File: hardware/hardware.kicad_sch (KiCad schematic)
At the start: 8 parts, among them J1 Conn_01x03_Pin, J2 Conn_01x03_Pin, J3 Conn_01x03_Pin, J4 Conn_01x03_Pin, J5 Conn_01x03_Pin, J6 Conn_01x04_Pin, U1 ESP32-DEVKITC-32D

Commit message: feat: hardware schematic
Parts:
- added C1: C_Polarized, symbol Device:C_Polarized
- added IR1, IR2: Conn_01x03_Pin, symbol Connector:Conn_01x03_Pin
- added L7805: L7805, Package_TO_SOT_THT:TO-220-3_Vertical, symbol Regulator_Linear:L7805
- added PW: Screw_Terminal_01x02, TerminalBlock:TerminalBlock_bornier-2_P5.08mm, symbol Connector:Screw_Terminal_01x02
- added TCS: Conn_01x06_Pin, symbol Connector:Conn_01x06_Pin
- added TIP3055: TIP3055G, Package_TO_SOT_THT:TO-247-3_Vertical, symbol Transistor_BJT:TIP3055G
- renumbered J6 to MP01, J1 to SM1, J2 to SM2, J3 to SM3, J4 to SM4, J5 to SM5
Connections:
- net at SM5.1 (Pin_1): now also U1.J2-15 (IO13)
- net at A1.2 (VDD), SM1.2 (Pin_2), SM2.2 (Pin_2)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: now also C1.1, IR1.1 (Pin_1), IR2.1 (Pin_1), TCS.1 (Pin_1), TIP3055.3 (E)
- net at A1.1 (GND), SM1.3 (Pin_3), SM2.3 (Pin_3)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: now also A1.7 (GND), C1.2, IR1.2 (Pin_2), IR2.2 (Pin_2), L7805.2 (GND), PW.2 (Pin_2), TCS.2 (Pin_2)
- net at SM3.1 (Pin_1): now also U1.J2-8 (IO33)
- net at SM1.1 (Pin_1): now also U1.J2-6 (IO35)
- net at A1.13 (~{RESET}): now also A1.14 (~{SLEEP})
- net at A1.15 (STEP): now also U1.J2-12 (IO14)
- net at A1.16 (DIR): now also U1.J2-13 (IO12)
- net at A1.8 (VMOT): now also L7805.1 (IN), PW.1 (Pin_1), TIP3055.2 (C)
- net at SM2.1 (Pin_1): now also U1.J2-7 (IO32)
- net at SM4.1 (Pin_1): now also U1.J2-11 (IO27)
- net at U1.J3-3 (IO22): now also TCS.4 (Pin_4)
- net at U1.J3-6 (IO21): now also TCS.5 (Pin_5)
- net at U1.J3-8 (IO19): now also IR1.3 (Pin_3)
- net at U1.J3-9 (IO18): now also IR2.3 (Pin_3)
- new net: L7805.3 (OUT), TIP3055.1 (B)
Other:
- moved on the sheet: A1, MP01, SM1, SM2, SM3, SM4, SM5, U1

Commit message: feat: added footprints
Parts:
- C1: footprint (none) -> Capacitor_THT:CP_Radial_D5.0mm_P2.50mm
- IR1, IR2, SM1, SM2, SM3, SM4, SM5: footprint (none) -> Connector_PinHeader_2.54mm:PinHeader_1x03_P2.54mm_Vertical
- MP1: renamed from MP01; footprint (none) -> Connector_PinHeader_2.54mm:PinHeader_1x04_P2.54mm_Vertical
- TCS1: renamed from TCS; footprint (none) -> Connector_PinHeader_2.54mm:PinHeader_1x06_P2.54mm_Vertical
- renumbered PW to PW1
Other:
- moved on the sheet: SM2
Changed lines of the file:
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@@
 (kicad_sch (version 20230121) (generator eeschema)
   (paper "A4")
-  (junction (at 59.69 64.77) (diameter 0) (color 0 0 0 0)
+  (junction (at 60.96 66.04) (diameter 0) (color 0 0 0 0)
   )
   (junction (at 152.4 132.08) (diameter 0) (color 0 0 0 0)
@@
   (junction (at 152.4 124.46) (diameter 0) (color 0 0 0 0)
   )
-  (junction (at 60.96 67.31) (diameter 0) (color 0 0 0 0)
-  )
   (junction (at 60.96 99.06) (diameter 0) (color 0 0 0 0)
   )
+  (junction (at 59.69 63.5) (diameter 0) (color 0 0 0 0)
+  )
   (junction (at 60.96 88.9) (diameter 0) (color 0 0 0 0)
   )
@@
     (stroke (width 0) (type default))
   )
-  (wire (pts (xy 60.96 67.31) (xy 60.96 78.74))
+  (wire (pts (xy 60.96 66.04) (xy 60.96 78.74))
     (stroke (width 0) (type default))
   )
@@
     (stroke (width 0) (type default))
   )
-  (wire (pts (xy 59.69 64.77) (xy 59.69 76.2))
+  (wire (pts (xy 59.69 63.5) (xy 59.69 76.2))
     (stroke (width 0) (type default))
   )
@@
     (stroke (width 0) (type default))
   )
-  (wire (pts (xy 60.96 67.31) (xy 60.96 55.88))
-    (stroke (width 0) (type default))
-  )
   (wire (pts (xy 58.42 123.19) (xy 58.42 119.38))
     (stroke (width 0) (type default))
@@
     (stroke (width 0) (type default))
   )
-  (wire (pts (xy 59.69 53.34) (xy 59.69 64.77))
+  (wire (pts (xy 59.69 53.34) (xy 59.69 63.5))
     (stroke (width 0) (type default))
   )
@@
     (stroke (width 0) (type default))
   )
-  (wire (pts (xy 59.69 64.77) (xy 57.15 64.77))
+  (wire (pts (xy 59.69 63.5) (xy 57.15 63.5))
     (stroke (width 0) (type default))
   )
@@
     (stroke (width 0) (type default))
   )
-  (wire (pts (xy 57.15 67.31) (xy 60.96 67.31))
+  (wire (pts (xy 57.15 66.04) (xy 60.96 66.04))
     (stroke (width 0) (type default))
   )
@@
     (stroke (width 0) (type default))
   )
+  (wire (pts (xy 60.96 66.04) (xy 60.96 55.88))
+    (stroke (width 0) (type default))
+  )
   (wire (pts (xy 86.36 58.42) (xy 119.38 58.42))
     (stroke (width 0) (type default))
@@
   )
   (wire (pts (xy 58.42 124.46) (xy 64.77 124.46))
-    (stroke (width 0) (type default))
-  )
-  (wire (pts (xy 57.15 60.96) (xy 57.15 62.23))
     (stroke (width 0) (type default))
   )
@@
   (symbol (lib_id "Connector:Conn_01x04_Pin") (at 52.07 120.65 0) (unit 1)
     (in_bom yes) (on_board yes) (dnp no) (fields_autoplaced)
-    (property "Reference" "MP01" (at 52.705 113.03 0)
+    (property "Reference" "MP1" (at 52.705 113.03 0)
       (effects (font (size 1.27 1.27)))
     )
@@
       (effects (font (size 1.27 1.27)) hide)
     )
-    (property "Footprint" "" (at 52.07 120.65 0)
+    (property "Footprint" "Connector_PinHeader_2.54mm:PinHeader_1x04_P2.54mm_Vertical" (at 52.07 120.65 0)
       (effects (font (size 1.27 1.27)) hide)
     )
@@
       (project "hardware"
         (path "/00a5c2e5-2a35-4d39-93f3-5a75c761c929"
-          (reference "MP01") (unit 1)
+          (reference "MP1") (unit 1)
         )
       )
@@
       (effects (font (size 1.27 1.27)) hide)
     )
-    (property "Footprint" "" (at 52.07 96.52 0)
+    (property "Footprint" "Connector_PinHeader_2.54mm:PinHeader_1x03_P2.54mm_Vertical" (at 52.07 96.52 0)
       (effects (font (size 1.27 1.27)) hide)
     )
@@
       (effects (font (size 1.27 1.27)) (justify right) hide)
     )
-    (property "Footprint" "" (at 179.07 78.74 0)
+    (property "Footprint" "Connector_PinHeader_2.54mm:PinHeader_1x03_P2.54mm_Vertical" (at 179.07 78.74 0)
       (effects (font (size 1.27 1.27)) hide)
     )
@@
   (symbol (lib_id "Connector:Conn_01x06_Pin") (at 52.07 35.56 0) (unit 1)
     (in_bom yes) (on_board yes) (dnp no)
-    (property "Reference" "TCS" (at 52.07 27.94 0)
+    (property "Reference" "TCS1" (at 52.07 27.94 0)
       (effects (font (size 1.27 1.27)))
     )
@@
       (effects (font (size 1.27 1.27)) hide)
     )
-    (property "Footprint" "" (at 52.07 35.56 0)
+    (property "Footprint" "Connector_PinHeader_2.54mm:PinHeader_1x06_P2.54mm_Vertical" (at 52.07 35.56 0)
       (effects (font (size 1.27 1.27)) hide)
     )
@@
       (project "hardware"
         (path "/00a5c2e5-2a35-4d39-93f3-5a75c761c929"
-          (reference "TCS") (unit 1)
+          (reference "TCS1") (unit 1)
         )
       )
@@
       (effects (font (size 1.27 1.27)) hide)
     )
-    (property "Footprint" "" (at 52.07 76.2 0)
+    (property "Footprint" "Connector_PinHeader_2.54mm:PinHeader_1x03_P2.54mm_Vertical" (at 52.07 76.2 0)
       (effects (font (size 1.27 1.27)) hide)
     )
@@
       (effects (font (size 1.27 1.27)) (justify right) hide)
     )
-    (property "Footprint" "" (at 179.07 67.31 0)
+    (property "Footprint" "Connector_PinHeader_2.54mm:PinHeader_1x03_P2.54mm_Vertical" (at 179.07 67.31 0)
       (effects (font (size 1.27 1.27)) hide)
     )
@@
   (symbol (lib_id "Connector:Screw_Terminal_01x02") (at 160.02 132.08 0) (unit 1)
     (in_bom yes) (on_board yes) (dnp no) (fields_autoplaced)
-    (property "Reference" "PW" (at 162.56 133.35 0)
+    (property "Reference" "PW1" (at 162.56 133.35 0)
       (effects (font (size 1.27 1.27)) (justify left))
     )
@@
       (project "hardware"
         (path "/00a5c2e5-2a35-4d39-93f3-5a75c761c929"
-          (reference "PW") (unit 1)
+          (reference "PW1") (unit 1)
         )
       )
@@
       (effects (font (size 1.27 1.27)) (justify left) hide)
     )
-    (property "Footprint" "" (at 112.7252 129.54 0)
+    (property "Footprint" "Capacitor_THT:CP_Radial_D5.0mm_P2.50mm" (at 112.7252 129.54 0)
       (effects (font (size 1.27 1.27)) hide)
     )
@@
       (effects (font (size 1.27 1.27)) hide)
     )
-    (property "Footprint" "" (at 52.07 53.34 0)
+    (property "Footprint" "Connector_PinHeader_2.54mm:PinHeader_1x03_P2.54mm_Vertical" (at 52.07 53.34 0)
       (effects (font (size 1.27 1.27)) hide)
     )
@@
     )
   )
-  (symbol (lib_id "Connector:Conn_01x03_Pin") (at 52.07 64.77 0) (unit 1)
+  (symbol (lib_id "Connector:Conn_01x03_Pin") (at 52.07 63.5 0) (unit 1)
     (in_bom yes) (on_board yes) (dnp no)
-    (property "Reference" "SM2" (at 52.07 59.69 0)
-      (effects (font (size 1.27 1.27)))
-    )
-    (property "Value" "Conn_01x03_Pin" (at 52.705 59.69 0)
-      (effects (font (size 1.27 1.27)) hide)
-    )
-    (property "Footprint" "" (at 52.07 64.77 0)
-      (effects (font (size 1.27 1.27)) hide)
-    )
-    (property "Datasheet" "~" (at 52.07 64.77 0)
+    (property "Reference" "SM2" (at 52.07 58.42 0)
+      (effects (font (size 1.27 1.27)))
+    )
+    (property "Value" "Conn_01x03_Pin" (at 52.705 58.42 0)
+      (effects (font (size 1.27 1.27)) hide)
+    )
+    (property "Footprint" "Connector_PinHeader_2.54mm:PinHeader_1x03_P2.54mm_Vertical" (at 52.07 63.5 0)
+      (effects (font (size 1.27 1.27)) hide)
+    )
+    (property "Datasheet" "~" (at 52.07 63.5 0)
       (effects (font (size 1.27 1.27)) hide)
     )
@@
       (effects (font (size 1.27 1.27)) hide)
     )
-    (property "Footprint" "" (at 52.07 86.36 0)
-      (effects (font (size 1.27 1.27)) hide)
-    )
+    (property "Footprint" "Connector_PinHeader_2.54mm:PinHeader_1x03_P2.54mm_Vertical" (at 52.07 86.36 0)
+      (effects (font (size 1.27 1.27)) hide)
+    )

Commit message: feat: pcb design
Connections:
- net at A1.1 (GND), A1.7 (GND), C1.2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: now also PW1.1 (Pin_1); no longer PW1.2 (Pin_2)
- net at A1.8 (VMOT), L7805.1 (IN), TIP3055.2 (C): now also PW1.2 (Pin_2); no longer PW1.1 (Pin_1)
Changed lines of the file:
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@@
   (junction (at 60.96 66.04) (diameter 0) (color 0 0 0 0)
   )
-  (junction (at 152.4 132.08) (diameter 0) (color 0 0 0 0)
-  )
   (junction (at 59.69 53.34) (diameter 0) (color 0 0 0 0)
   )
+  (junction (at 152.4 134.62) (diameter 0) (color 0 0 0 0)
+  )
   (junction (at 105.41 99.06) (diameter 0) (color 0 0 0 0)
   )
@@
   (junction (at 60.96 78.74) (diameter 0) (color 0 0 0 0)
   )
-  (junction (at 128.27 134.62) (diameter 0) (color 0 0 0 0)
-  )
   (junction (at 78.74 99.06) (diameter 0) (color 0 0 0 0)
   )
@@
   (junction (at 102.87 144.78) (diameter 0) (color 0 0 0 0)
   )
+  (junction (at 128.27 132.08) (diameter 0) (color 0 0 0 0)
+  )
   (junction (at 59.69 76.2) (diameter 0) (color 0 0 0 0)
   )
@@
     (stroke (width 0) (type default))
   )
-  (wire (pts (xy 152.4 124.46) (xy 152.4 132.08))
-    (stroke (width 0) (type default))
-  )
   (wire (pts (xy 171.45 69.85) (xy 173.99 69.85))
     (stroke (width 0) (type default))
@@
     (stroke (width 0) (type default))
   )
-  (wire (pts (xy 152.4 132.08) (xy 152.4 142.24))
-    (stroke (width 0) (type default))
-  )
-  (wire (pts (xy 128.27 134.62) (xy 154.94 134.62))
+  (wire (pts (xy 152.4 124.46) (xy 152.4 134.62))
+    (stroke (width 0) (type default))
+  )
+  (wire (pts (xy 128.27 132.08) (xy 154.94 132.08))
     (stroke (width 0) (type default))
   )
@@
     (stroke (width 0) (type default))
   )
-  (wire (pts (xy 152.4 132.08) (xy 154.94 132.08))
-    (stroke (width 0) (type default))
-  )
   (wire (pts (xy 60.96 88.9) (xy 60.96 78.74))
     (stroke (width 0) (type default))
@@
     (stroke (width 0) (type default))
   )
+  (wire (pts (xy 152.4 134.62) (xy 152.4 142.24))
+    (stroke (width 0) (type default))
+  )
   (wire (pts (xy 162.56 38.1) (xy 57.15 38.1))
     (stroke (width 0) (type default))
@@
     (stroke (width 0) (type default))
   )
+  (wire (pts (xy 152.4 134.62) (xy 154.94 134.62))
+    (stroke (width 0) (type default))
+  )

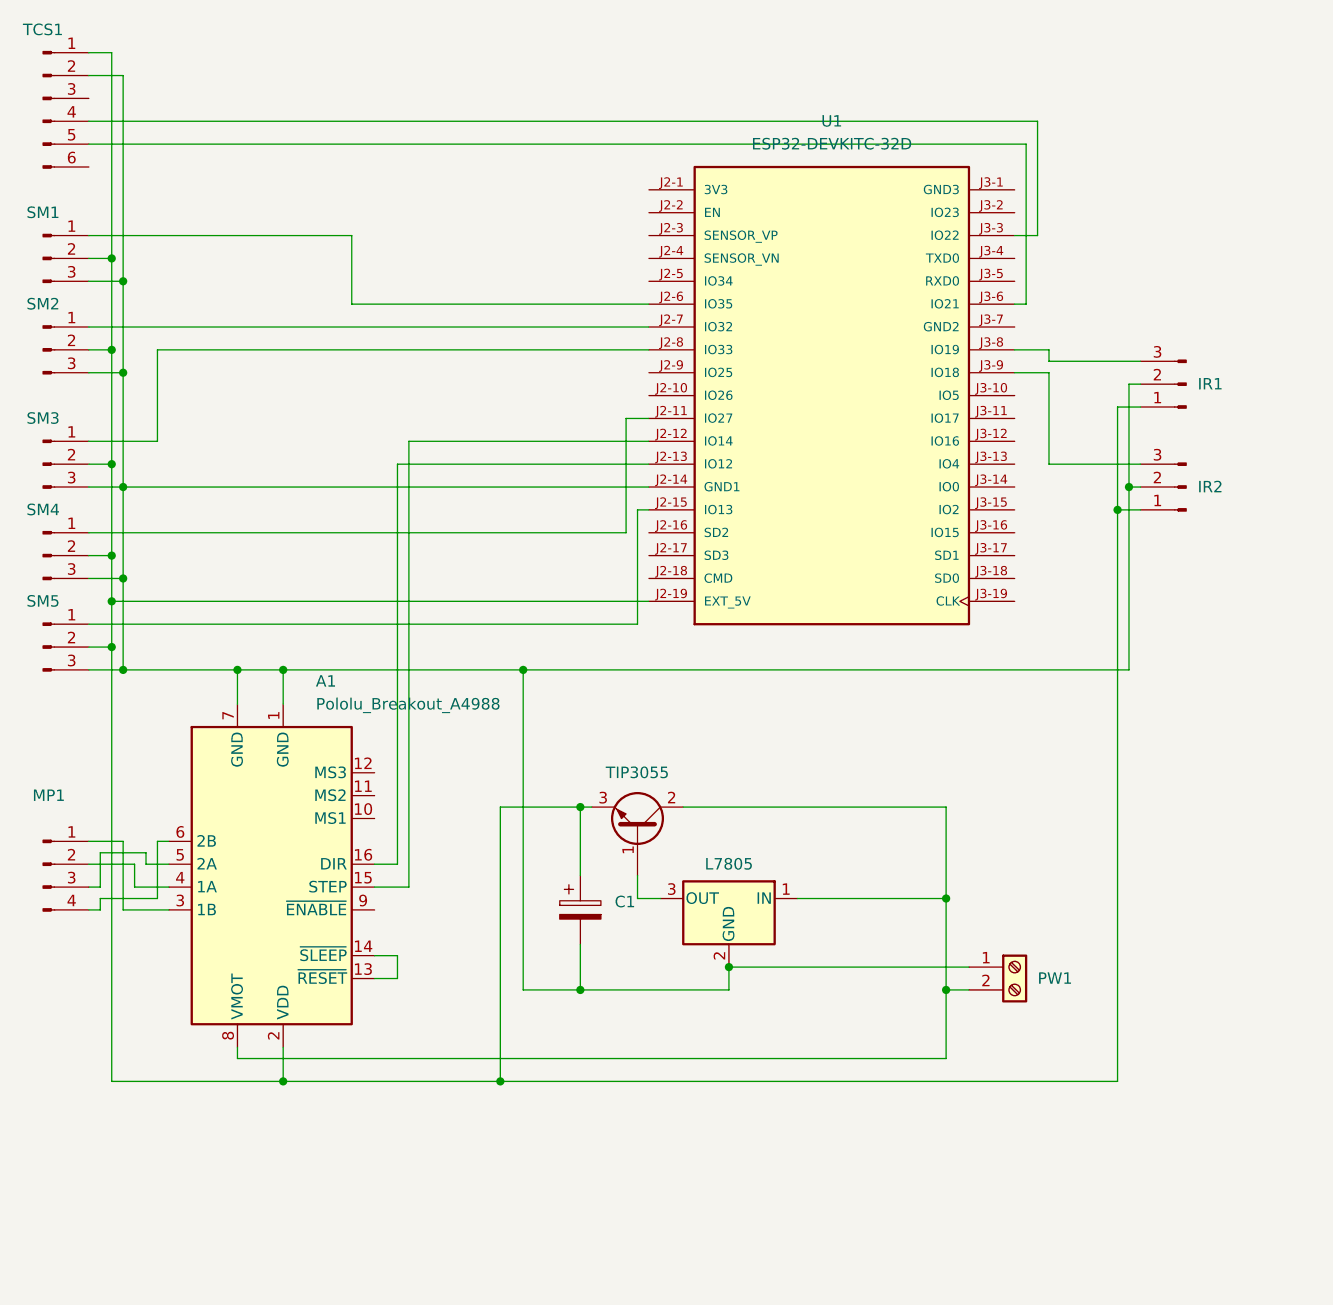
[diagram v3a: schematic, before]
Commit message: refactor: changed a4988
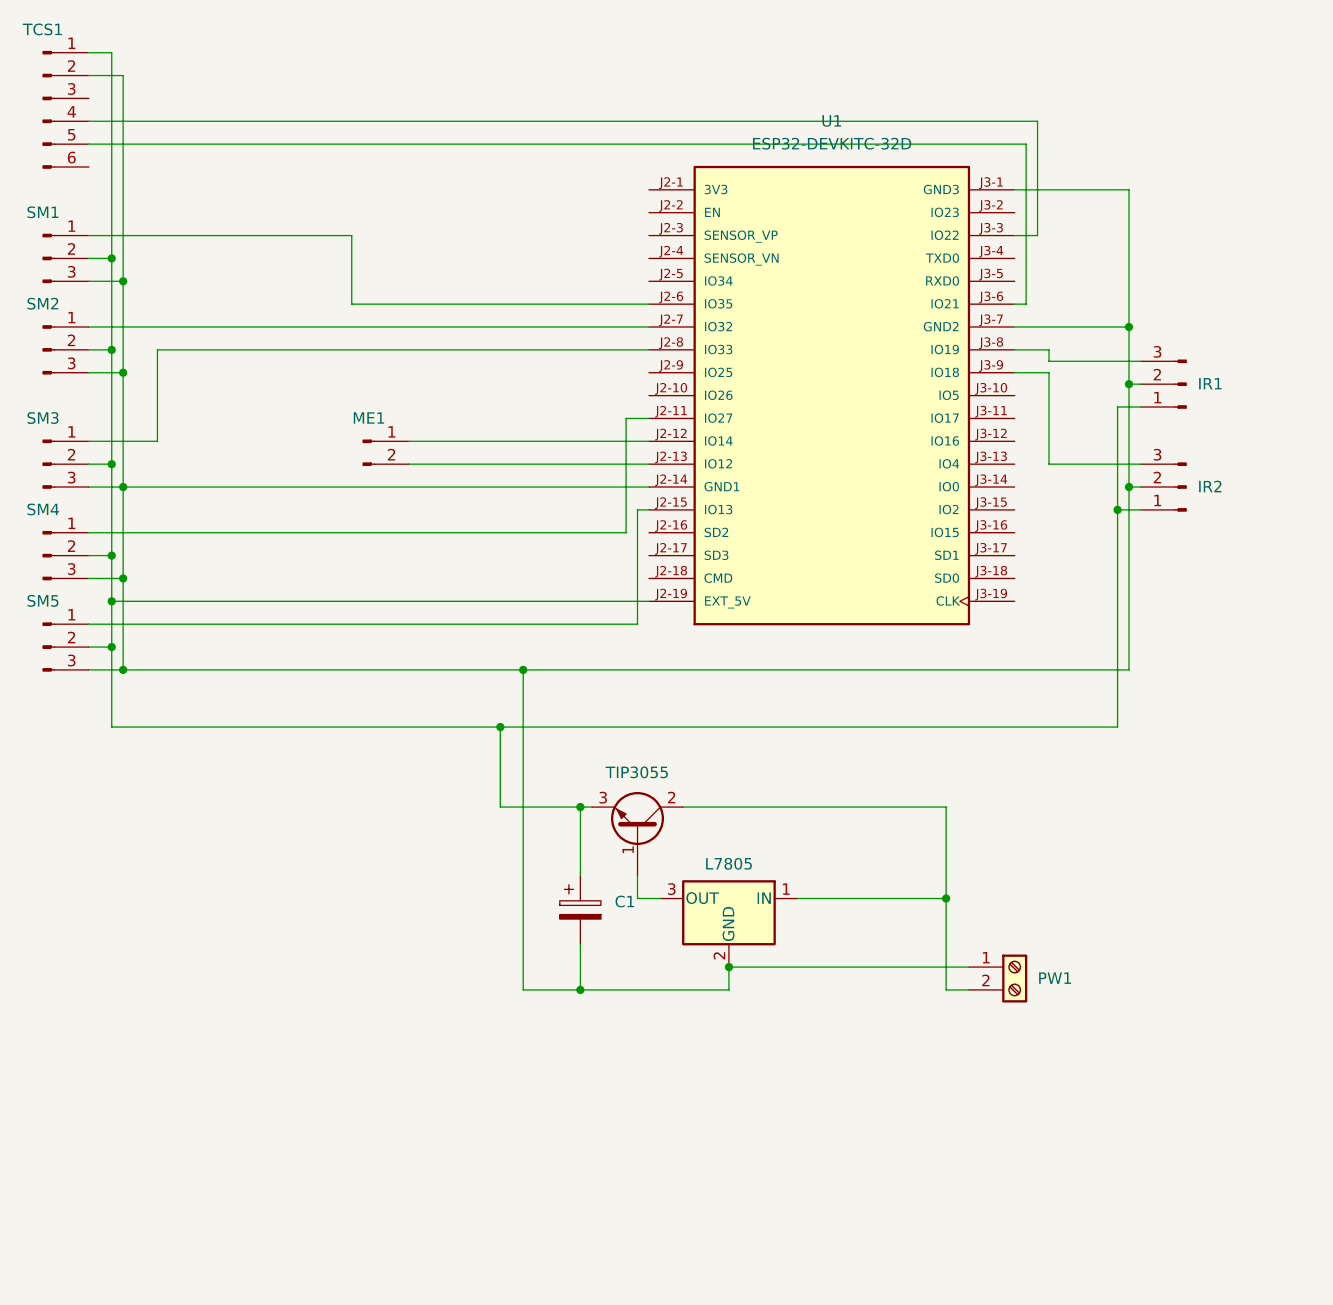
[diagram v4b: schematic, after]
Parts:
- removed A1: Pololu_Breakout_A4988, Module:Pololu_Breakout-16_15.2x20.3mm, symbol Driver_Motor:Pololu_Breakout_A4988
- removed MP1: Conn_01x04_Pin, Connector_PinHeader_2.54mm:PinHeader_1x04_P2.54mm_Vertical, symbol Connector:Conn_01x04_Pin
- added ME1: Conn_01x02_Pin, Connector_PinHeader_2.54mm:PinHeader_1x02_P2.54mm_Vertical, symbol Connector:Conn_01x02_Pin
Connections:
- net at C1.2, IR1.2 (Pin_2), IR2.2 (Pin_2)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: now also U1.J3-1 (GND3), U1.J3-7 (GND2)
- net at U1.J2-12 (IO14): now also ME1.1 (Pin_1)
- net at U1.J2-13 (IO12): now also ME1.2 (Pin_2)
